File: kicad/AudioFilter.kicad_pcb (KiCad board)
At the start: 2 copper layers, 92.5 x 54.3 mm, 60 parts, among them J1 Conn_01x02_Pin, J10 Conn_01x02_Pin, J2 Conn_01x02_Pin, J3 Conn_01x02_Pin, J4 Conn_01x04_Pin, J5 Conn_01x02_Pin, J6 Conn_01x03_Pin, J7 Conn_01x04_Pin, J8 Conn_01x04_Pin, J9 Conn_01x07_Pin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

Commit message: Some tidying up
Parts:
- renumbered R21 to R20, R24 to R21
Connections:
- J2 pad 1: /P1.2 -> GND
- J2 pad 2: GND -> /P1.2
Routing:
- net /P1.2: track 9.35 -> 4.49 mm
- net GND: track 181.9 -> 179.6 mm
- net /THRU: track 148.4 -> 148.9 mm
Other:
- board text added: "+ - G"
- board text added: "1 2 3 4 5 6 C"
- board text added: "2 5 6 C"
- board text added: "3 5 6 C"
- board text added: "Audio Multi Filter V0.1 acramonics 2026"
- board text added: "C100Ka"
- board text added: "C100Kb"
- board text added: "C10K Pot"
- board text added: "Input"
- board text added: "OUT"
- board text added: "POWER"
- board text added: "S G"
- board text added: "SW1a SW1b"
- board text added: "Wafer2"
- board text added: "Wafer3"

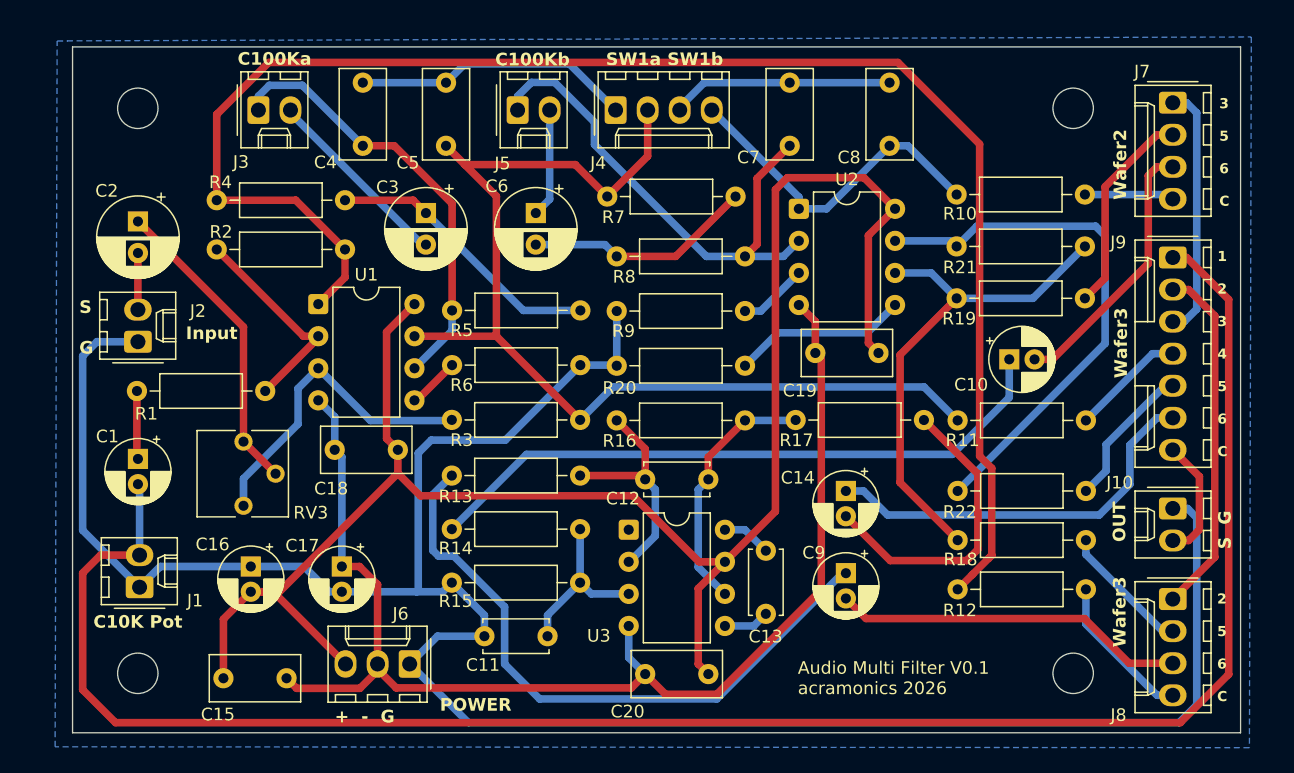
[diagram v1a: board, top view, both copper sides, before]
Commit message: Component size adjustments
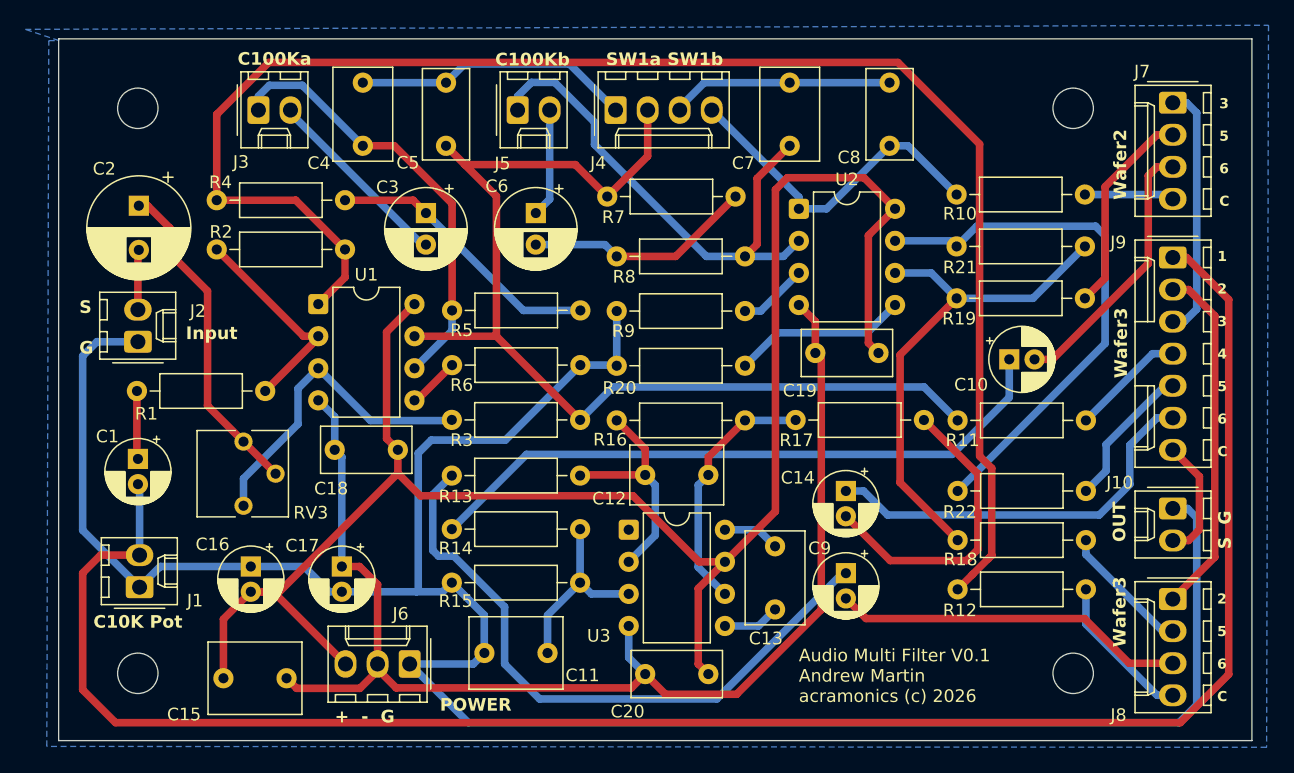
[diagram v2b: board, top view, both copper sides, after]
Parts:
- C1: value 1uF -> 1uF 16V A
- C10, C9: value 10uF -> 10uF 16V
- C11: value 47pF -> 47pF PP; footprint Capacitor_THT:C_Disc_D5.0mm_W2.5mm_P5.00mm -> Capacitor_THT:C_Rect_L7.2mm_W5.5mm_P5.00mm_FKS2_FKP2_MKS2_MKP2
- C12, C13: value 47pF -> 47pF PP; footprint Capacitor_THT:C_Disc_D5.0mm_W2.5mm_P5.00mm -> Capacitor_THT:C_Rect_L7.2mm_W4.5mm_P5.00mm_FKS2_FKP2_MKS2_MKP2
- C15: footprint Capacitor_THT:C_Rect_L7.0mm_W3.5mm_P5.00mm -> Capacitor_THT:C_Rect_L7.2mm_W5.5mm_P5.00mm_FKS2_FKP2_MKS2_MKP2
- C16, C17: value 10uF -> 10uF 25V
- C2: value 220uF -> 220uF 25V A; footprint Capacitor_THT:CP_Radial_D6.3mm_P2.50mm -> Capacitor_THT:CP_Radial_D8.0mm_P3.50mm
- C3, C6: value 100uF -> 100uF 25V A
- C4, C7: value 100nF -> 100nF PP; footprint Capacitor_THT:C_Rect_L7.0mm_W3.5mm_P5.00mm -> Capacitor_THT:C_Rect_L7.2mm_W4.5mm_P5.00mm_FKS2_FKP2_MKS2_MKP2
- C5, C8: value 6.8nF -> 6.8nF PP
- moved C11 1.33 mm to (125.5, 125.6)
- moved C2 1.24 mm to (98.2, 90.1)
- moved C13 0.81 mm to (148.6, 117.1)
- moved C12 0.35 mm to (138.3, 111.5)
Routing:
- net Net-(C2-Pad1): track 24.5 -> 26.1 mm
- net Net-(U3-+): track 13.8 -> 15.1 mm
- net -15V: track 100.7 -> 101.6 mm
- net Net-(U3-COMP): track 3.64 -> 4.51 mm
- net GND: track 179.6 -> 180.3 mm
- net Net-(U3-C/B): track 3.93 -> 4.51 mm
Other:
- board size 92.5 x 54.3 mm -> 94.5 x 55.6 mm
- board text added: "Audio Multi Filter V0.1 Andrew Martin acramonics (c) 2026"
- board text removed: "Audio Multi Filter V0.1 acramonics 2026"
